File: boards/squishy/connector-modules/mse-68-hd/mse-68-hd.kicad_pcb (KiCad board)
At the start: 6 copper layers, 75 x 55 mm, 18 parts, among them J1 SCSI PHY Mezz, J2 Conn_02x25_Odd_Even, J3 Conn_01x04, U1 M24C02-RMC

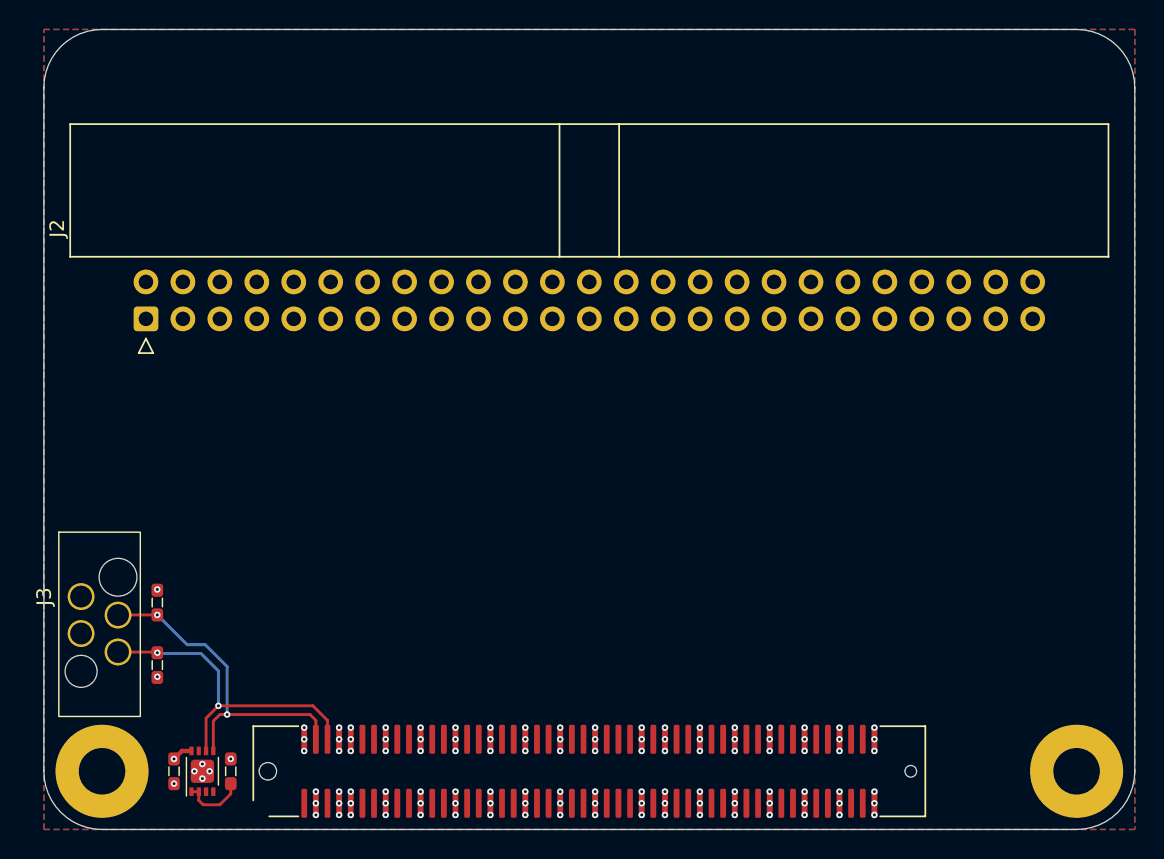
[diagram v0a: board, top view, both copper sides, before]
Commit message: squishy: connectors: Defined the impedance requirements, adjusted the stackup, and shortened the board for the 68-pin HD LVD/MSE/SE connector module
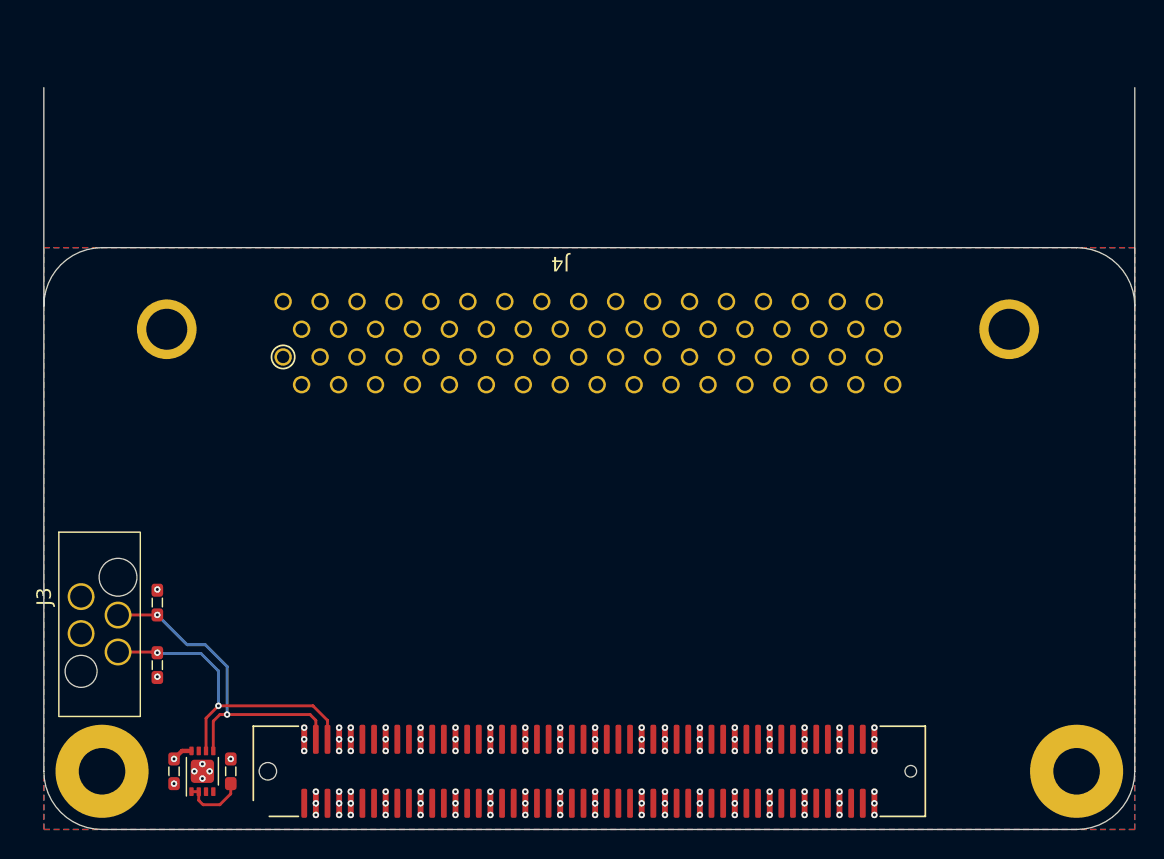
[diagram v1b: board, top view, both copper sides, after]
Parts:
- removed J2: Conn_02x25_Odd_Even, Connector_IDC:IDC-Header_2x25_P2.54mm_Horizontal
- added J4: Conn_02x34_Clockwise_Shield, lethalbit-connectors:5787082-7, F.Cu at (145.5, 106.5)
- moved REF** 15.0 mm to (121.0, 99.8)
- moved REF** 15.0 mm to (174.0, 99.8)
- moved REF** 11.3 mm to (109.8, 110.0)
- moved REF** 11.2 mm to (185.2, 110.0)
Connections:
- J1 pad 11: /CON.DP12+ -> /CON.DB12+
- J1 pad 12: /CON.DP12- -> /CON.DB12-
- J1 pad 17: /CON.DP14+ -> /CON.DB14+
- J1 pad 18: /CON.DP14- -> /CON.DB14-
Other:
- board size 75 x 55 mm -> 75 x 51 mm
- board text added: "0.2028mm"
- board text added: "0.2104mm"
- board text added: "0.4000mm"
- board text added: "IFF JLCPCB: JLC06161H-7628"
- board text added: "Impedance Table: 50Ω Coplanar Single Ended (inner): width: TODO 72Ω Coplanar Single Ended (outter): width: 0.1115mm 72Ω Non-Coplanar Single Ended (outter): width: 0.1514mm 50Ω Non-Coplanar Single Ended (inner): width: TODO 120Ω Coplanar Differential (outter): width: 0.1148, space: 0.2mm 120Ω Non-Coplanar Differential (outter): width: 0.1275, space: 0.2mm"
- board text added: "Outter Copper: 1oz Inner Copper: 0.5oz"
- board text added: "Prepreg (7628*1)"
- board text removed: "0.0994mm"
- board text removed: "0.1088mm"
- board text removed: "0.5500mm"
- board text removed: "IFF JLCPCB: JLC06161H-3313"
- board text removed: "Impedance Table: 50Ω Coplanar Signle Ended (inner): width: TODO 50Ω Coplanar Signle Ended (outter): width: TODO 50Ω Non-Coplanar Signle Ended (inner): width: TODO 50Ω Non-Coplanar Signle Ended (outter): width: TODO"
- board text removed: "Outter Copper: 1Oz Inner Copper: 0.5Oz"
- board text removed: "Prepreg (2116*1)"
- board text removed: "Prepreg (3313*1)"

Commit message: squishy: connectors: Routed out the first half of the HVD/LVD/SE 68-pin connector module
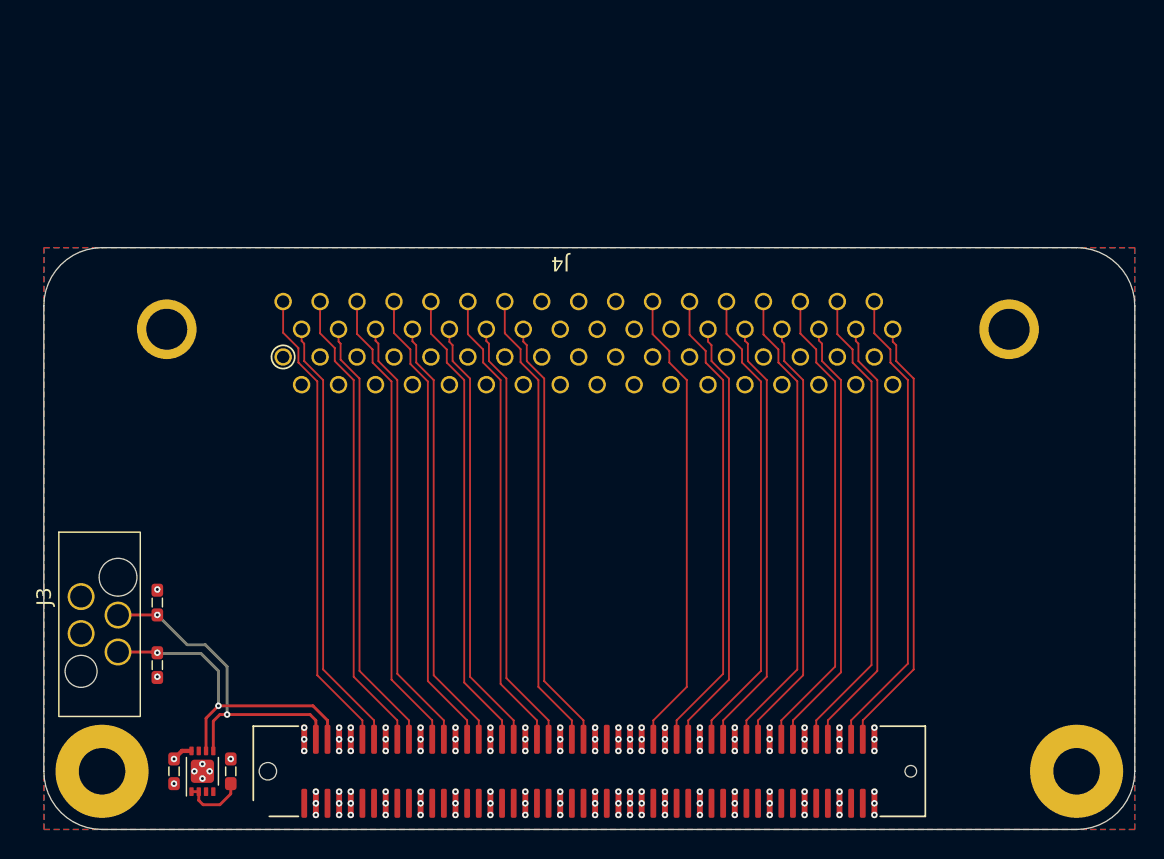
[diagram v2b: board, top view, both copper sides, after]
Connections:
- J4 pad 58: /CON.ATN- -> /CON.ACK-
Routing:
- net /CON.DB10-: track 0.00 -> 32.7 mm
- net /CON.DB8-: track 0.00 -> 32.6 mm
- net /CON.REQ-: track 0.00 -> 32.6 mm
- net /CON.SEL-: track 0.00 -> 32.5 mm
- net /CON.RST-: track 0.00 -> 32.5 mm
- net /CON.BSY-: track 0.00 -> 32.4 mm
- net /CON.DB12-: track 0.00 -> 32.4 mm
- net /CON.DB14-: track 0.00 -> 32.3 mm
- net /CON.DP1-: track 0.00 -> 32.2 mm
- net /CON.DB1-: track 0.00 -> 32.2 mm
- net /CON.DB3-: track 0.00 -> 32.1 mm
- net /CON.DB5-: track 0.00 -> 32.1 mm
- net /CON.ATN-: track 0.00 -> 32.0 mm
- net /CON.DB7-: track 0.00 -> 32.0 mm
- net /CON.DB13-: track 0.00 -> 30.3 mm
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- added copper zone on In2.Cu, net +3V3
- added copper zone on In2.Cu, net /CON.TERMPWR
- removed copper zone on In1.Cu, net +3V3
- removed copper zone on In2.Cu, net GND
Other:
- board size 75 x 51 mm -> 75 x 40 mm

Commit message: squishy: connectors: Routed out the rest of the connector, shortening the board to 34mm, and began length matching
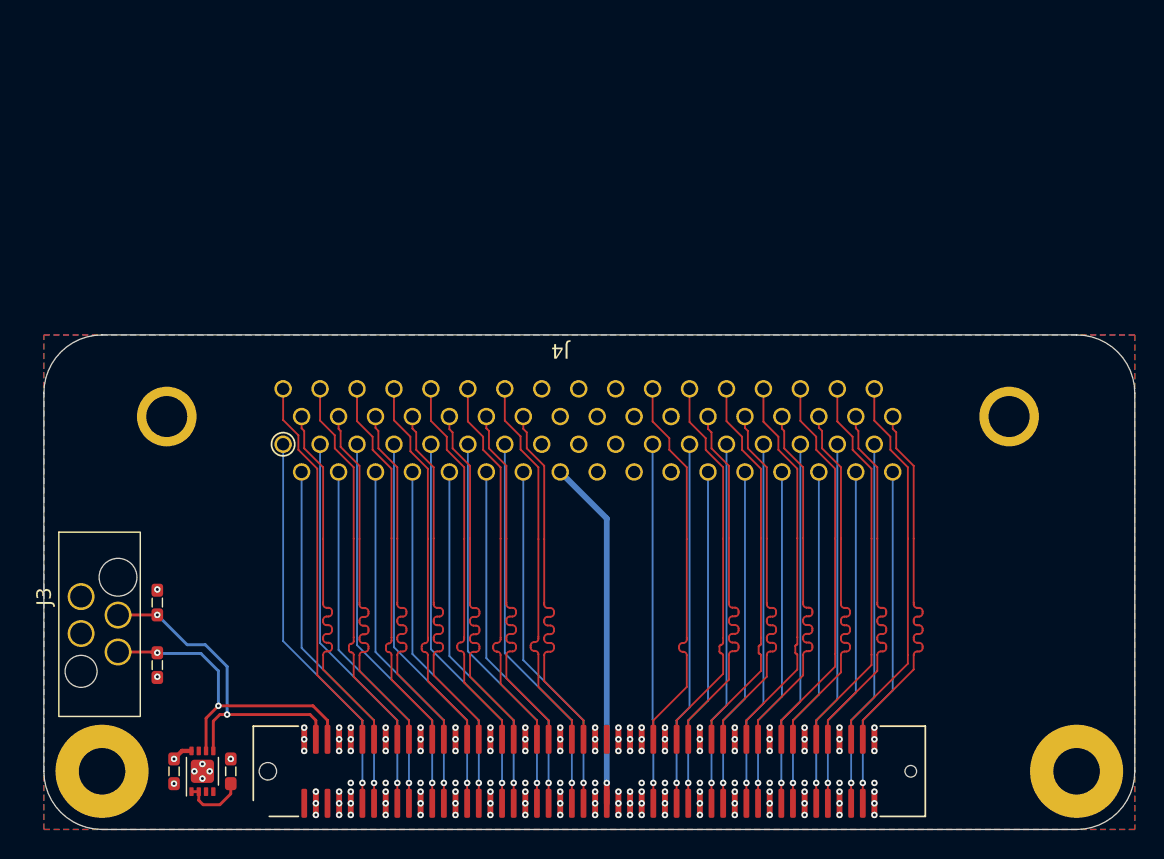
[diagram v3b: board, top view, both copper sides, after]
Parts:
- moved J4 6.00 mm to (145.5, 112.5)
- moved REF** 6.00 mm to (121.0, 105.8)
- moved REF** 6.00 mm to (174.0, 105.8)
- moved REF** 5.00 mm to (109.8, 115.0)
- moved REF** 5.00 mm to (185.2, 115.0)
- moved REF** 4.75 mm to (185.2, 131.0)
- moved REF** 4.75 mm to (109.7, 131.0)
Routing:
- net /CON.DB12+: track 0.00 -> 26.9 mm, vias 0 -> 1
- net /CON.DB14+: track 0.00 -> 26.9 mm, vias 0 -> 1
- net /CON.DP1+: track 0.00 -> 26.8 mm, vias 0 -> 1
- net /CON.DB1+: track 0.00 -> 26.8 mm, vias 0 -> 1
- net /CON.DB3+: track 0.00 -> 26.7 mm, vias 0 -> 1
- net /CON.DB5+: track 0.00 -> 26.7 mm, vias 0 -> 1
- net /CON.DB7+: track 0.00 -> 26.6 mm, vias 0 -> 1
- net /CON.DB10+: track 0.00 -> 25.3 mm, vias 0 -> 1
- net /CON.DB8+: track 0.00 -> 25.3 mm, vias 0 -> 1
- net /CON.REQ+: track 0.00 -> 25.2 mm, vias 0 -> 1
- net /CON.SEL+: track 0.00 -> 25.2 mm, vias 0 -> 1
- net /CON.RST+: track 0.00 -> 25.1 mm, vias 0 -> 1
- net /CON.BSY+: track 0.00 -> 25.1 mm, vias 0 -> 1
- net /CON.DB13+: track 0.00 -> 24.8 mm, vias 0 -> 1
- net /CON.DB15+: track 0.00 -> 24.8 mm, vias 0 -> 1
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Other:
- board size 75 x 40 mm -> 75 x 34 mm

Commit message: squishy: connectors: Completed length matchinig and added sheild handling to the 68-pin HD LVD/MSE/SE connector module
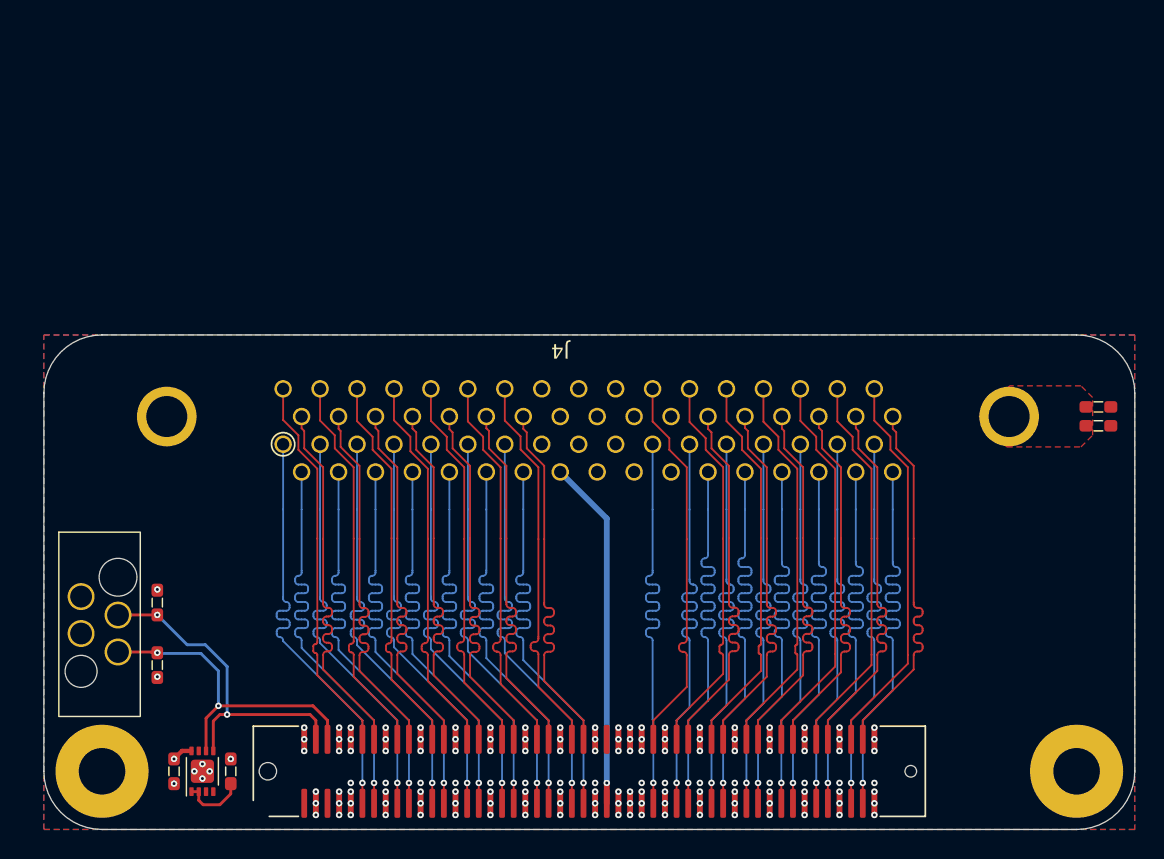
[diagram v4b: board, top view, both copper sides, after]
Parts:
- added C2: 100n, rhais_rcl:C0603, F.Cu at (182.5, 111.0)
- added R4: 1M, rhais_rcl:R0603, F.Cu at (182.5, 112.2)
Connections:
- J4 pad SHIELD: unconnected-(J4-PadSHIELD) -> /SHIELD
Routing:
- net /CON.ACK+: track 23.3 -> 29.4 mm
- net /CON.MSG+: track 23.4 -> 29.4 mm
- net /CON.C/D+: track 23.5 -> 29.4 mm
- net /CON.I/O+: track 23.5 -> 29.4 mm
- net /CON.DB9+: track 23.6 -> 29.4 mm
- net /CON.DB11+: track 23.6 -> 29.4 mm
- net /CON.DP0+: track 24.5 -> 29.4 mm
- net /CON.DB6+: track 24.6 -> 29.4 mm
- net /CON.DB4+: track 24.6 -> 29.4 mm
- net /CON.DB2+: track 24.7 -> 29.4 mm
- net /CON.ATN+: track 24.7 -> 29.4 mm
- net /CON.DB0+: track 24.7 -> 29.4 mm
- net /CON.DB15+: track 24.8 -> 29.4 mm
- net /CON.DB13+: track 24.8 -> 29.4 mm
- net /CON.BSY+: track 25.1 -> 29.4 mm
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- added copper zone on F.Cu, net /SHIELD
